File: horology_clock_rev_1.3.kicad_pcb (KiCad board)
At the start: 2 copper layers, 100 x 100 mm, 42 parts, among them J1 Conn_01x36, J10 Conn_01x08, J11 Screw_Terminal_01x02, J12 Conn_01x02, J13 Conn_01x04, J14 Conn_01x10, J2 Conn_01x36, J3 Screw_Terminal_01x02, J4 Screw_Terminal_01x02, J5 Screw_Terminal_01x02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

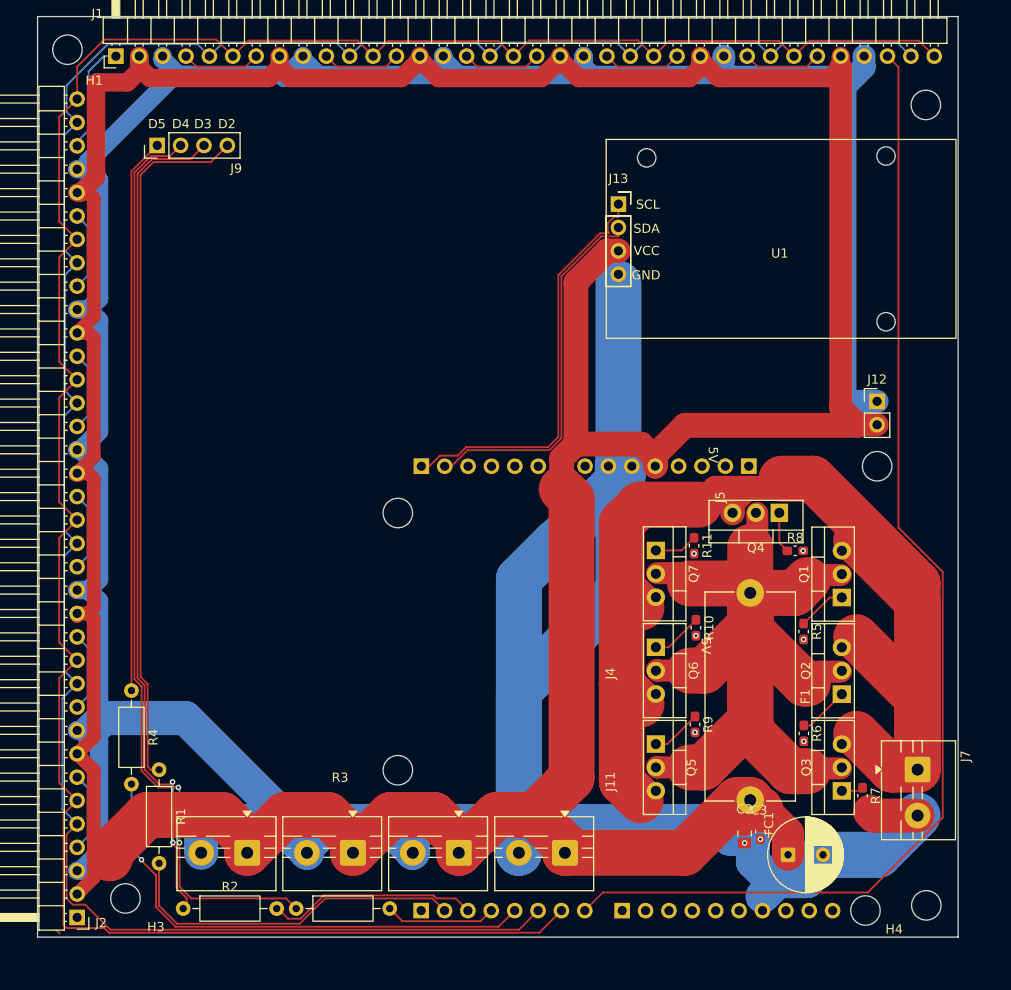
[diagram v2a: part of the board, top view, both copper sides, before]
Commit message: Corrected Power Order: Now POWER -> FUSE -> MOSFETS
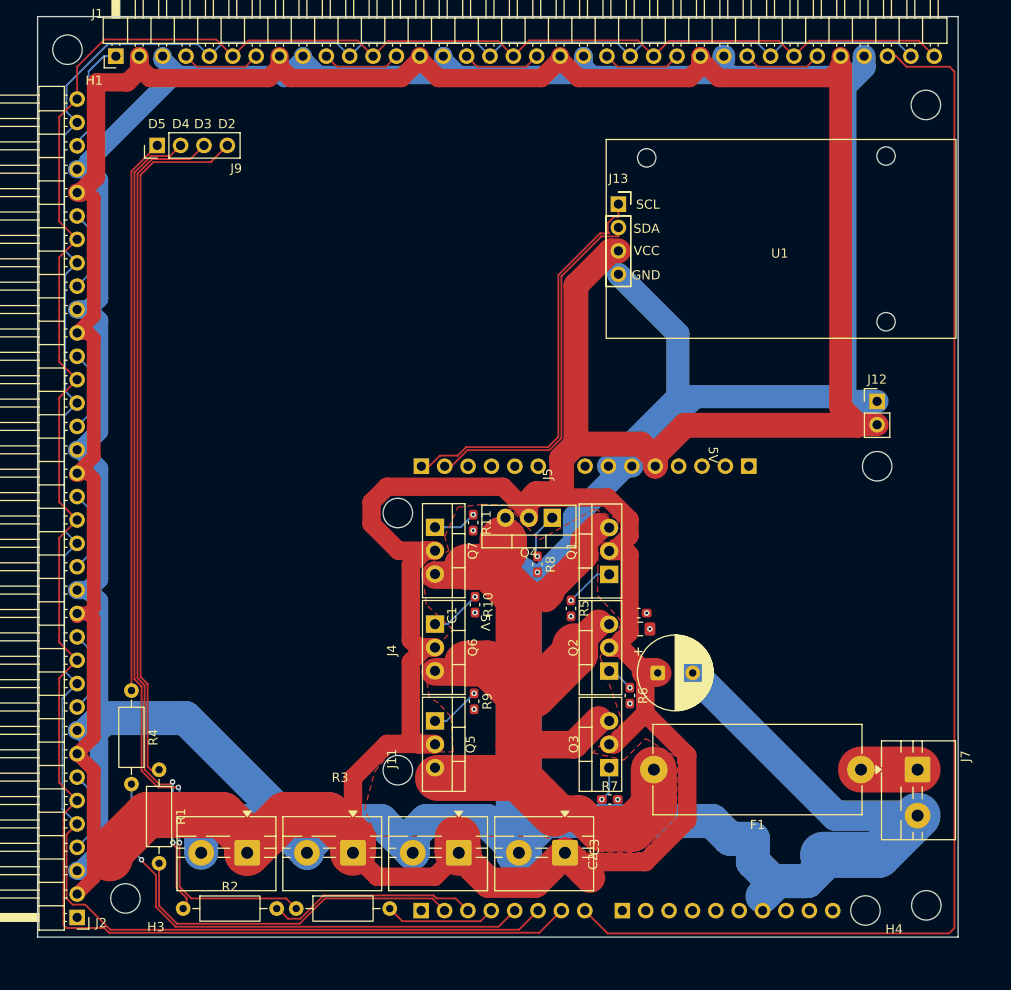
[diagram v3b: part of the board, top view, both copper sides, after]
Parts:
- moved R8 28.0 mm to (135.2, 108.7), turned to -90 degrees
- moved R7 27.5 mm to (143.1, 134.2), turned to 0 degrees
- moved C3 27.1 mm to (146.3, 114.0), turned to 0 degrees
- moved Q1 25.4 mm to (143.1, 109.8)
- moved Q2 25.4 mm to (143.1, 120.3)
- moved Q3 25.4 mm to (143.1, 130.8)
- moved R5 25.4 mm to (138.9, 113.5)
- moved C2 24.9 mm to (146.4, 115.7), turned to 0 degrees
- moved Q4 24.7 mm to (136.9, 103.6)
- moved C1 24.3 mm to (148.3, 120.5)
- moved Q5 24.1 mm to (124.1, 125.7)
- moved Q6 24.1 mm to (124.1, 115.2)
- moved Q7 24.1 mm to (124.1, 104.7)
- moved R10 24.1 mm to (128.5, 113.1)
- moved R11 24.1 mm to (128.3, 104.2)
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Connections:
- F1 pad 1: VIN_PROTECTED -> VIN_RAW
- F1 pad 2: +5V -> VIN_PROTECTED
- Q1 pad 2: VIN_PROTECTED -> +5V
- Q1 pad 3: VIN_RAW -> VIN_PROTECTED
- Q2 pad 2: VIN_PROTECTED -> +5V
- Q2 pad 3: VIN_RAW -> VIN_PROTECTED
- Q3 pad 2: VIN_PROTECTED -> +5V
- Q3 pad 3: VIN_RAW -> VIN_PROTECTED
- Q4 pad 2: VIN_PROTECTED -> +5V
- Q4 pad 3: VIN_RAW -> VIN_PROTECTED
- Q5 pad 2: VIN_PROTECTED -> +5V
- Q5 pad 3: VIN_RAW -> VIN_PROTECTED
- Q6 pad 2: VIN_PROTECTED -> +5V
- Q6 pad 3: VIN_RAW -> VIN_PROTECTED
- Q7 pad 2: VIN_PROTECTED -> +5V
- Q7 pad 3: VIN_RAW -> VIN_PROTECTED
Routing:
- net VIN_RAW: track 152.9 -> 6.15 mm
- net +5V: track 445.3 -> 528.8 mm
- net GND: track 482.2 -> 524.6 mm, vias 8 -> 9
- net MAX_DIN: track 128.3 -> 142.4 mm
- net VIN_PROTECTED: track 119.5 -> 111.1 mm
- net Net-(Q2-G): track 5.53 -> 3.00 mm, vias 0 -> 1
- net Net-(Q3-G): track 2.39 -> 3.77 mm, vias 0 -> 1
- net unconnected-(J14-GND_L-Pad2): track 0.56 -> 0.00 mm
- net Net-(Q4-G): track 4.48 -> 5.00 mm, vias 0 -> 1
- net Net-(Q5-G): vias 0 -> 1
- net Net-(Q7-G): vias 0 -> 1
- net Net-(Q6-G): vias 0 -> 1
- net Net-(Q1-G): vias 0 -> 1
- added copper zone on F.Cu, net VIN_PROTECTED

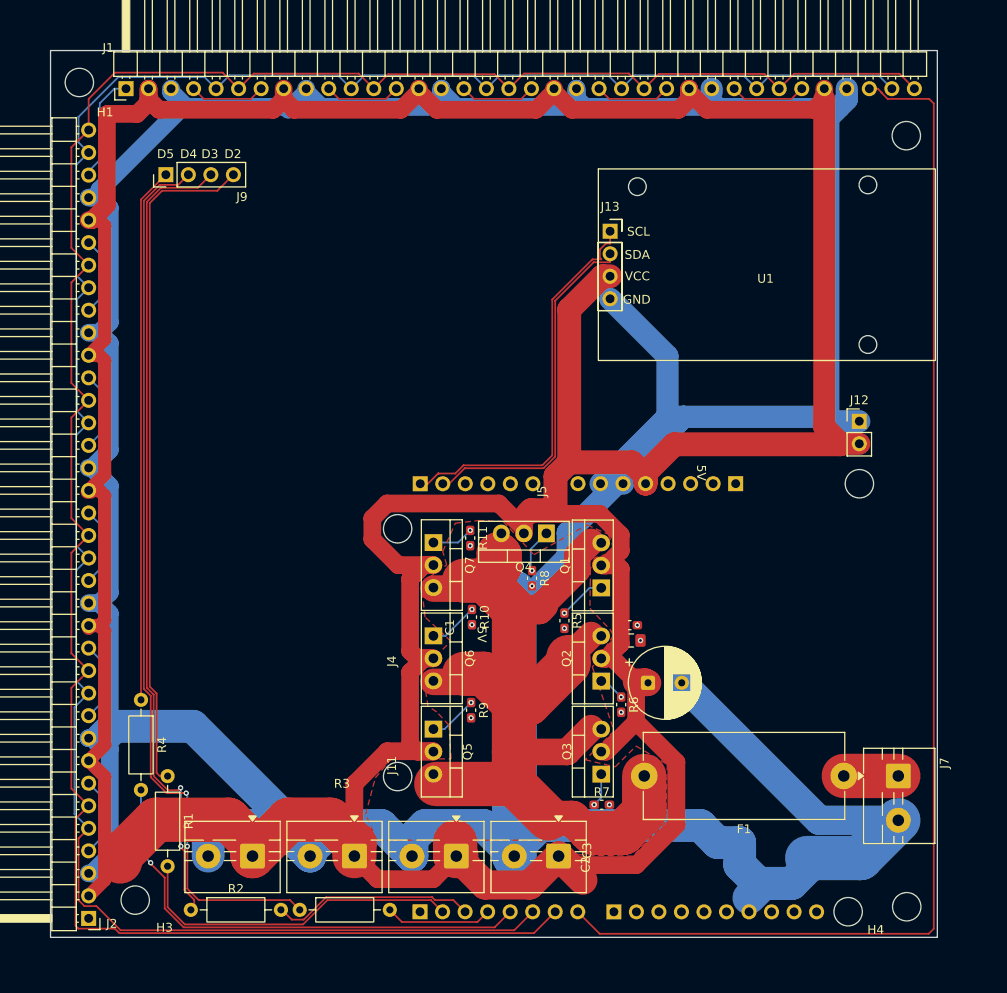
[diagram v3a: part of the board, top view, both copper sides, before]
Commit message: Added silkscreen component identifiers.
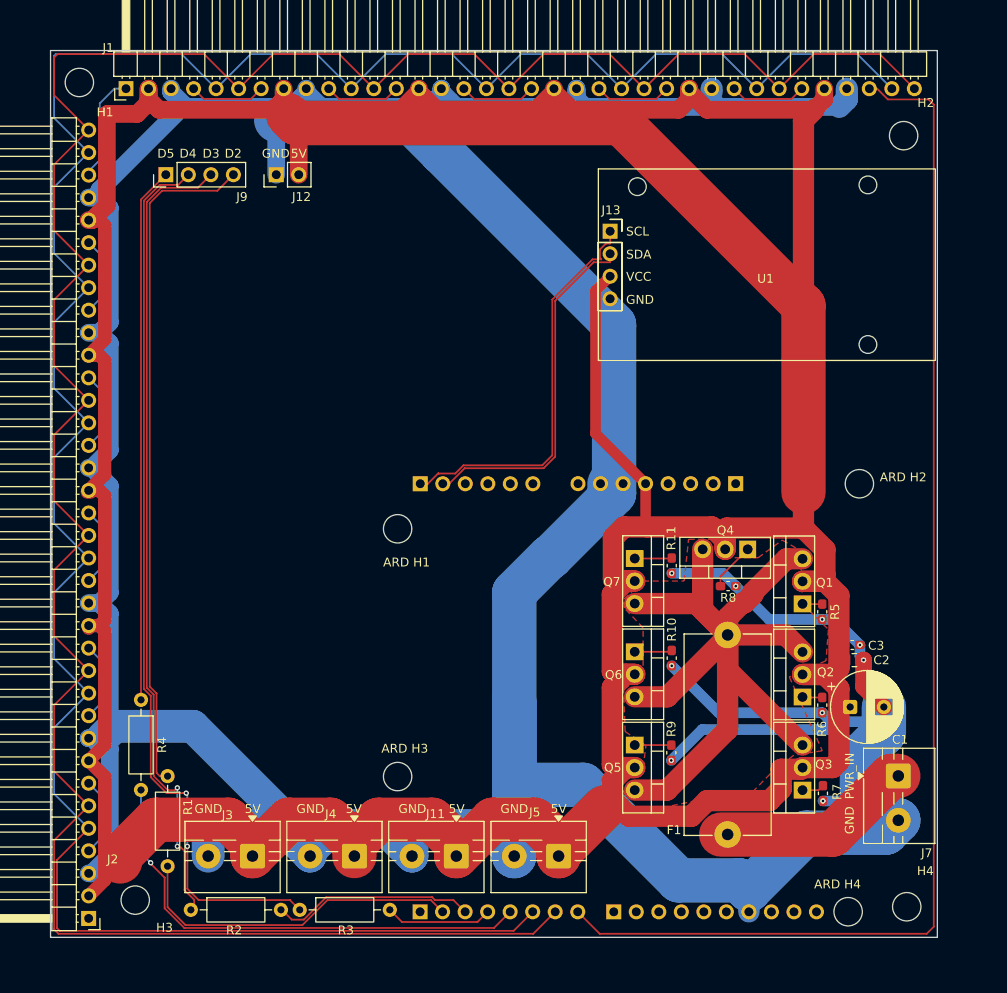
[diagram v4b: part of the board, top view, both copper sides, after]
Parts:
- moved J12 71.4 mm to (106.4, 63.2), turned to 90 degrees
- moved R5 29.1 mm to (168.0, 112.5)
- moved C2 25.3 mm to (171.6, 117.9)
- moved C3 25.2 mm to (171.4, 116.2)
- moved R7 25.0 mm to (168.1, 133.0), turned to -90 degrees
- moved R9 23.1 mm to (150.9, 128.4)
- moved R10 23.0 mm to (151.0, 117.7)
- moved C1 23.0 mm to (171.1, 123.2)
- moved R11 22.9 mm to (151.0, 107.3)
- moved Q1 22.8 mm to (165.8, 111.6)
- moved Q2 22.8 mm to (165.8, 122.1)
- moved Q3 22.8 mm to (165.8, 132.6)
- moved Q4 22.8 mm to (159.6, 105.4)
- moved Q5 22.8 mm to (146.8, 127.5)
- moved Q6 22.8 mm to (146.8, 117.0)
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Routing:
- net GND: track 524.6 -> 595.9 mm
- net +5V: track 528.8 -> 581.2 mm
- net MAX_CS: track 249.0 -> 284.6 mm
- net MAX_CLK: track 259.4 -> 290.4 mm
- net VIN_RAW: track 6.15 -> 22.7 mm
- net VIN_PROTECTED: track 111.1 -> 98.6 mm
- net Net-(Q1-G): track 5.32 -> 2.24 mm, vias 1 -> 0
- net Net-(Q5-G): track 5.49 -> 4.13 mm, vias 1 -> 0
- net Net-(Q6-G): track 5.58 -> 4.24 mm, vias 1 -> 0
- net Net-(Q3-G): track 3.77 -> 2.51 mm, vias 1 -> 0
- net Net-(Q2-G): track 3.00 -> 2.25 mm, vias 1 -> 0
- net Net-(Q7-G): track 4.72 -> 4.20 mm, vias 1 -> 0
- net Net-(Q4-G): track 5.00 -> 5.42 mm, vias 1 -> 0
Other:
- board text added: "05/03/2026"
- board text added: "1/1"
- board text added: "ARD H1"
- board text added: "ARD H2"
- board text added: "ARD H3"
- board text added: "ARD H4"
- board text added: "ARDUNIO UNO R3"
- board text added: "H4"
- board text added: "J3"
- board text added: "J8"
- board text added: "PWR_IN"
- board text added: "Power Distribution and Control PCB"

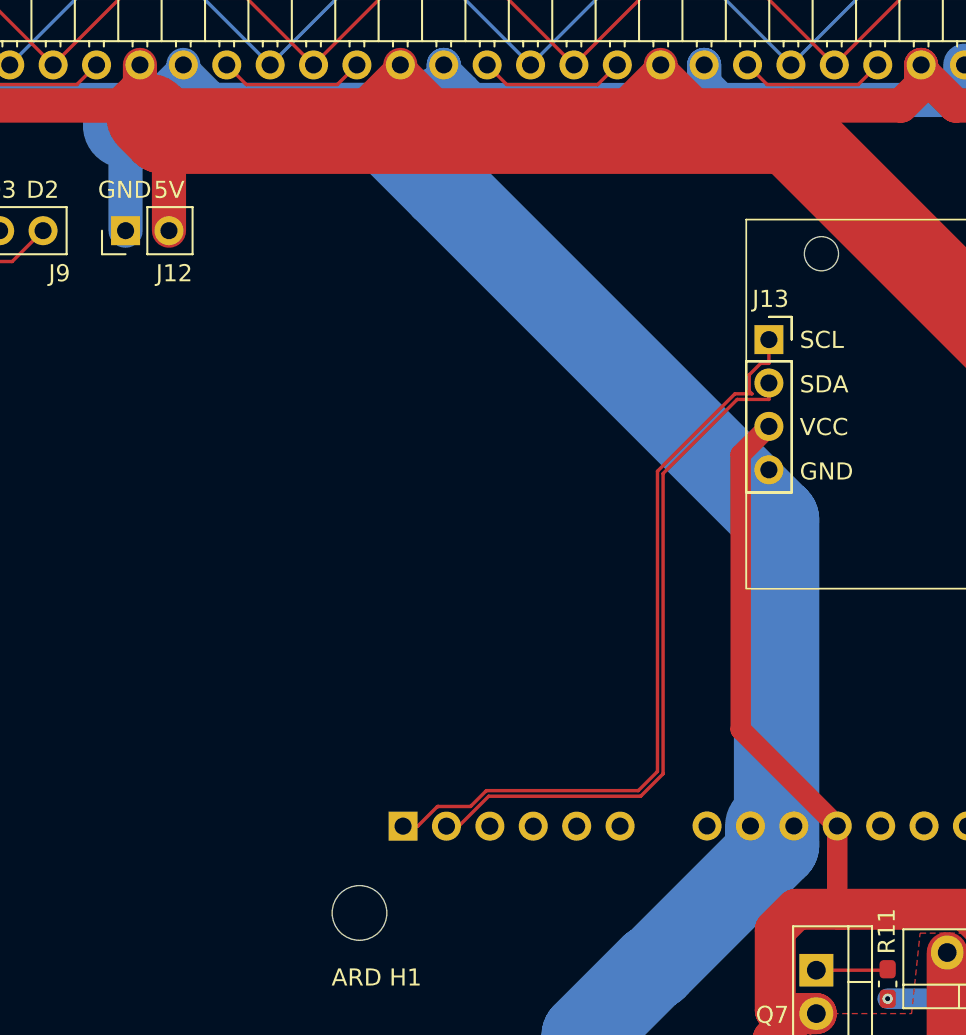
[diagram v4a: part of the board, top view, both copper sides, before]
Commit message: Adjusted some traces.
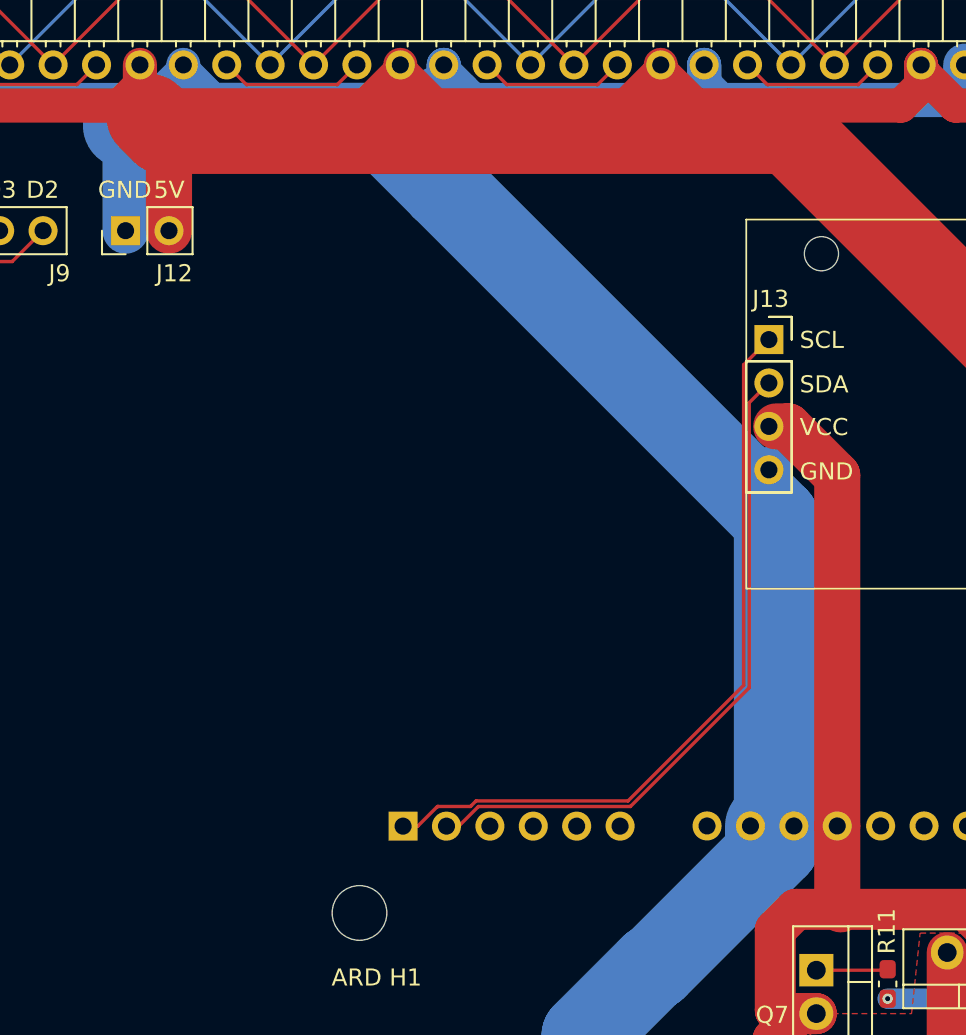
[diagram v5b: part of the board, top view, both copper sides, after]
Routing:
- net +5V: track 581.2 -> 611.1 mm
- net GND: track 595.9 -> 599.0 mm
- net RTC_SDA: track 40.5 -> 39.4 mm
- net RTC_SCL: track 45.2 -> 44.2 mm
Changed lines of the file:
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@@
 	)
 	(footprint "MountingHole:MountingHole_3.2mm_M3"
+		(locked yes)
 		(layer "F.Cu")
 		(at 84.2 52.8)
@@
 	)
 	(footprint "MountingHole:MountingHole_3.2mm_M3"
+		(locked yes)
 		(layer "F.Cu")
 		(at 177.5 145.75)
@@
 	)
 	(segment
+		(start 148.05 98.04)
+		(end 148.05 77.521473)
+		(width 2.7)
+		(layer "F.Cu")
+		(net 4)
+	)
+	(segment
 		(start 85.141999 129.4)
 		(end 85.371999 129.4)
@@
 	)
 	(segment
+		(start 145.183527 74.655)
+		(end 144.477 74.655)
+		(width 2.7)
+		(layer "F.Cu")
+		(net 4)
+	)
+	(segment
 		(start 152.96 53.860553)
 		(end 152.96 53.5)
@@
 	)
 	(segment
-		(start 142.399 76.306)
-		(end 142.399 92.389)
-		(width 1.2)
-		(layer "F.Cu")
-		(net 4)
-	)
-	(segment
 		(start 144.297 131.550217)
 		(end 144.297 133.644481)
@@
 	)
 	(segment
-		(start 144.05 74.655)
-		(end 142.399 76.306)
-		(width 1.2)
-		(layer "F.Cu")
-		(net 4)
-	)
-	(segment
 		(start 167.023081 55.879)
 		(end 154.978447 55.879)
@@
 	)
 	(segment
+		(start 144.05 74.655)
+		(end 148.15 78.755)
+		(width 1.2)
+		(layer "F.Cu")
+		(net 4)
+	)
+	(segment
 		(start 146.825 109.021349)
 		(end 145.789868 109.021349)
@@
 	)
 	(segment
+		(start 148.15 78.755)
+		(end 148.15 97.94)
+		(width 1.2)
+		(layer "F.Cu")
+		(net 4)
+	)
+	(segment
 		(start 169.15 119.557349)
 		(end 165.75 119.557349)
@@
 	)
 	(segment
-		(start 148.05 98.04)
-		(end 148.05 102.719349)
-		(width 1.2)
-		(layer "F.Cu")
-		(net 4)
-	)
-	(segment
 		(start 145.789868 119.539349)
 		(end 144.297 121.032217)
@@
 	)
 	(segment
+		(start 148.05 102.719349)
+		(end 148.05 98.04)
+		(width 2.7)
+		(layer "F.Cu")
+		(net 4)
+	)
+	(segment
 		(start 130.8094 135.939)
 		(end 135.538999 135.939)
@@
 	)
 	(segment
-		(start 148.05 102.719349)
-		(end 148.25 102.919349)
-		(width 1.2)
+		(start 148.05 77.521473)
+		(end 145.183527 74.655)
+		(width 2.7)
 		(layer "F.Cu")
 		(net 4)
@@
 	)
 	(segment
+		(start 148.15 97.94)
+		(end 148.05 98.04)
+		(width 1.2)
+		(layer "F.Cu")
+		(net 4)
+	)
+	(segment
 		(start 107.24 54.702081)
 		(end 108.416919 55.879)
@@
 	)
 	(segment
+		(start 108.94 63.2)
+		(end 108.94 57.681873)
+		(width 2.7)
+		(layer "F.Cu")
+		(net 4)
+	)
+	(segment
 		(start 126.7084 138.640001)
 		(end 126.7084 140.04)
@@
 	)
 	(segment
-		(start 142.399 92.389)
-		(end 148.05 98.04)
-		(width 1.2)
+		(start 108.94 57.681873)
+		(end 108.637127 57.379)
+		(width 2.7)
 		(layer "F.Cu")
 		(net 4)
@@
 	)
 	(segment
+		(start 148.25 102.919349)
+		(end 148.05 102.719349)
+		(width 2.7)
+		(layer "F.Cu")
+		(net 4)
+	)
+	(segment
 		(start 152.96 54.702081)
 		(end 151.783081 55.879)
@@
 	)
 	(segment
+		(start 144.05 79.676873)
+		(end 144.05 77.195)
+		(width 2.7)
+		(layer "B.Cu")
+		(net 5)
+	)
+	(segment
 		(start 145.51 98.04)
 		(end 144.05 96.58)
@@
 	)
 	(segment
+		(start 106.4 63.2)
+		(end 106.4 57.05)
+		(width 2.7)
+		(layer "B.Cu")
+		(net 5)
+	)
+	(segment
 		(start 176.55 136)
 		(end 175.150001 137.399999)
@@
 	)
 	(segment
+		(start 144.499 80.125873)
+		(end 144.05 79.676873)
+		(width 2.7)
+		(layer "B.Cu")
+		(net 5)
+	)
+	(segment
 		(start 87.629 82.201919)
 		(end 87.629 94.246553)
@@
 	)
 	(segment
-		(start 106.4 57.05)
-		(end 106.4 63.2)
-		(width 2)
-		(layer "B.Cu")
-		(net 5)
-	)
-	(segment
 		(start 172.449 128.620728)
 		(end 172.449 133.878898)
@@
 	)
 	(segment
-		(start 127.65 96.3)
-		(end 136.542843 96.3)
-		(width 0.2)
-		(layer "F.Cu")
-		(net 7)
-	)
-	(segment
-		(start 137.857473 77.413816)
-		(end 142.19429 73.077)
+		(start 125.9 98.05)
+		(end 127.05 96.9)
 		(width 0.2)
 		(layer "F.Cu")
@@
 	)
 	(segment
-		(start 125.18 98.05)
-		(end 125.9 98.05)
+		(start 127.05 96.9)
+		(end 135.942843 96.9)
 		(width 0.2)
 		(layer "F.Cu")
@@
 	)
 	(segment
-		(start 137.857473 94.985371)
-		(end 137.857473 77.413816)
+		(start 142.899 89.943843)
+		(end 142.899 73.266)
 		(width 0.2)
 		(layer "F.Cu")
@@
 	)
 	(segment
-		(start 136.542843 96.3)
-		(end 137.857473 94.985371)
+		(start 125.18 98.05)
+		(end 125.9 98.05)
 		(width 0.2)
 		(layer "F.Cu")
@@
 	)
 	(segment
-		(start 144.05 73.077)
+		(start 142.899 73.266)
 		(end 144.05 72.115)
 		(width 0.2)
@@
 	)
 	(segment
-		(start 142.19429 73.077)
-		(end 144.05 73.077)
-		(width 0.2)
-		(layer "F.Cu")
-		(net 7)
-	)
-	(segment
-		(start 125.9 98.05)
-		(end 127.65 96.3)
+		(start 135.942843 96.9)
+		(end 142.899 89.943843)
 		(width 0.2)
 		(layer "F.Cu")
@@
 	)
 	(segment
-		(start 127.514138 95.972)
-		(end 136.406981 95.972)
-		(width 0.2)
-		(layer "F.Cu")
-		(net 12)
-	)
-	(segment
-		(start 122.64 98.05)
-		(end 123.5 98.05)
-		(width 0.2)
-		(layer "F.Cu")
-		(net 12)
-	)
-	(segment
-		(start 142.899 71.63824)
-		(end 143.57324 70.964)
-		(width 0.2)
-		(layer "F.Cu")
-		(net 12)
-	)
-	(segment
-		(start 142.899 72.59176)
-		(end 142.899 71.63824)
-		(width 0.2)
-		(layer "F.Cu")
-		(net 12)
-	)
-	(segment
-		(start 136.406981 95.972)
-		(end 137.529473 94.849509)
+		(start 124.70324 96.899)
+		(end 126.587138 96.899)
 		(width 0.2)
 		(layer "F.Cu")
@@
 	)
 	(segment
-		(start 123.5 98.05)
-		(end 124.65 96.9)
+		(start 126.587138 96.899)
+		(end 126.914138 96.572)
 		(width 0.2)
 		(layer "F.Cu")
@@
 	)
 	(segment
-		(start 143.57324 70.964)
-		(end 144.05 70.964)
+		(start 142.571 89.807981)
+		(end 142.571 71.054)
 		(width 0.2)
 		(layer "F.Cu")
@@
 	)
 	(segment
-		(start 142.058428 72.749)
-		(end 143.05624 72.749)
+		(start 122.64 98.05)
+		(end 123.5 98.05)
 		(width 0.2)
 		(layer "F.Cu")
@@
 	)
 	(segment
-		(start 124.70324 96.899)
-		(end 126.587138 96.899)
+		(start 124.65 96.9)
+		(end 124.70224 96.9)
 		(width 0.2)
 		(layer "F.Cu")
@@
 	)
 	(segment
-		(start 144.05 70.964)
+		(start 142.571 71.054)
 		(end 144.05 69.575)
 		(width 0.2)
@@
 	)
 	(segment
-		(start 143.05624 72.749)
-		(end 142.899 72.59176)
+		(start 123.5 98.05)
+		(end 124.65 96.9)
 		(width 0.2)
 		(layer "F.Cu")
@@
 	)
 	(segment
-		(start 137.529473 77.277954)
-		(end 142.058428 72.749)
+		(start 135.806981 96.572)
+		(end 142.571 89.807981)
 		(width 0.2)
 		(layer "F.Cu")
@@
 	)
 	(segment
-		(start 137.529473 94.849509)
-		(end 137.529473 77.277954)
-		(width 0.2)
-		(layer "F.Cu")
-		(net 12)
-	)
-	(segment
-		(start 126.587138 96.899)
-		(end 127.514138 95.972)
-		(width 0.2)
-		(layer "F.Cu")
-		(net 12)
-	)
-	(segment
-		(start 124.65 96.9)
-		(end 124.70224 96.9)
+		(start 126.914138 96.572)
+		(end 135.806981 96.572)
 		(width 0.2)
 		(layer "F.Cu")
